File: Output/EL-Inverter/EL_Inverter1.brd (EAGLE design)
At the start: 20 x 13 mm, 13 parts

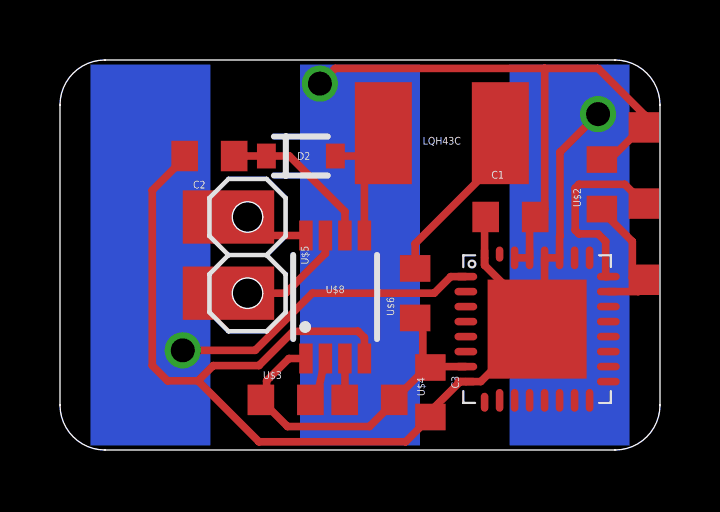
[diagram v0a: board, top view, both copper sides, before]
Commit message: Update Pinheader
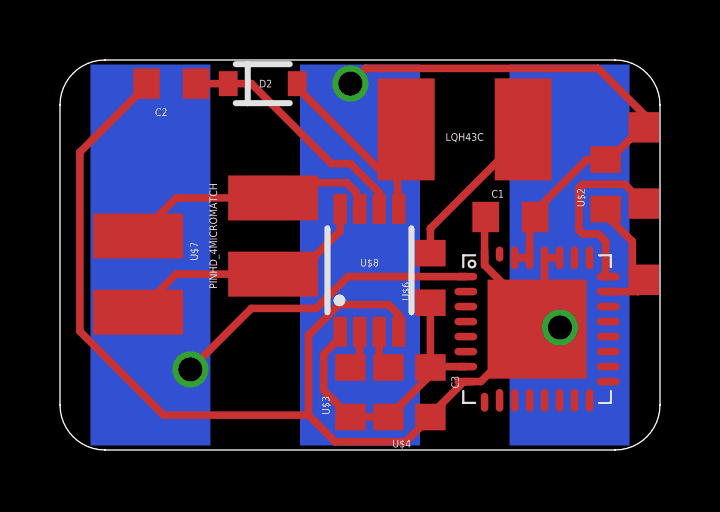
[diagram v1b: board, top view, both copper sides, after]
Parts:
- removed U$5: PINHD_22.54MOD, thar:PINHD_2_MOD
- added U$7: PINHD_4MICROMATCH, thar:MICROMATCH4P0L
- moved C2 2.73 mm to (5.46, 13.5)
- moved D2 2.73 mm to (8.51, 13.5)
- moved U$3 2.17 mm to (11.4, 3.17), turned to 90 degrees
- moved U$8 1.45 mm to (12.1, 7.24)
- moved LQH43C 0.77 mm to (15.2, 11.9)
- moved U$6 0.72 mm to (14.1, 6.99)
- moved U$4 0.68 mm to (12.7, 3.17), turned to 90 degrees
- moved U$2 0.13 mm to (19.9, 10.1)
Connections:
- net N$14: now also U$7.P$1, U$7.P$2; no longer U$5.P$1
- net N$16: now also U$7.P$3, U$7.P$4; no longer U$5.P$2
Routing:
- net N$14: track 2.84 -> 8.60 mm
- net N$16: track 4.38 -> 9.10 mm
- net N$6: track 5.26 -> 8.24 mm
- net N$7: track 6.18 -> 8.87 mm
- net GND: track 56.3 -> 58.6 mm
- net VCC: track 28.3 -> 26.3 mm
- net N$13: track 12.3 -> 10.7 mm
- net N$12: track 14.0 -> 14.7 mm
